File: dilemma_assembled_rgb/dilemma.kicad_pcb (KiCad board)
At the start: 4 copper layers, 130 x 91 mm, 122 parts, among them J1 USB_C_Receptacle_USB2.0, J102 Serial, J105 Conn_01x04_Female, J113 Cirque, J2 Conn_01x03_Female, J5 Conn_01x02, SW1 SW_Push, SW110 SW_SPST, SW2 SW_Push, SW3002 RotaryEncoder_Switch, U1 RP2040, U2 GD25Q80CEIGR, U3 XC6210B332MR-G, U4 USBLC6-2P6, Y1 Crystal_GND24

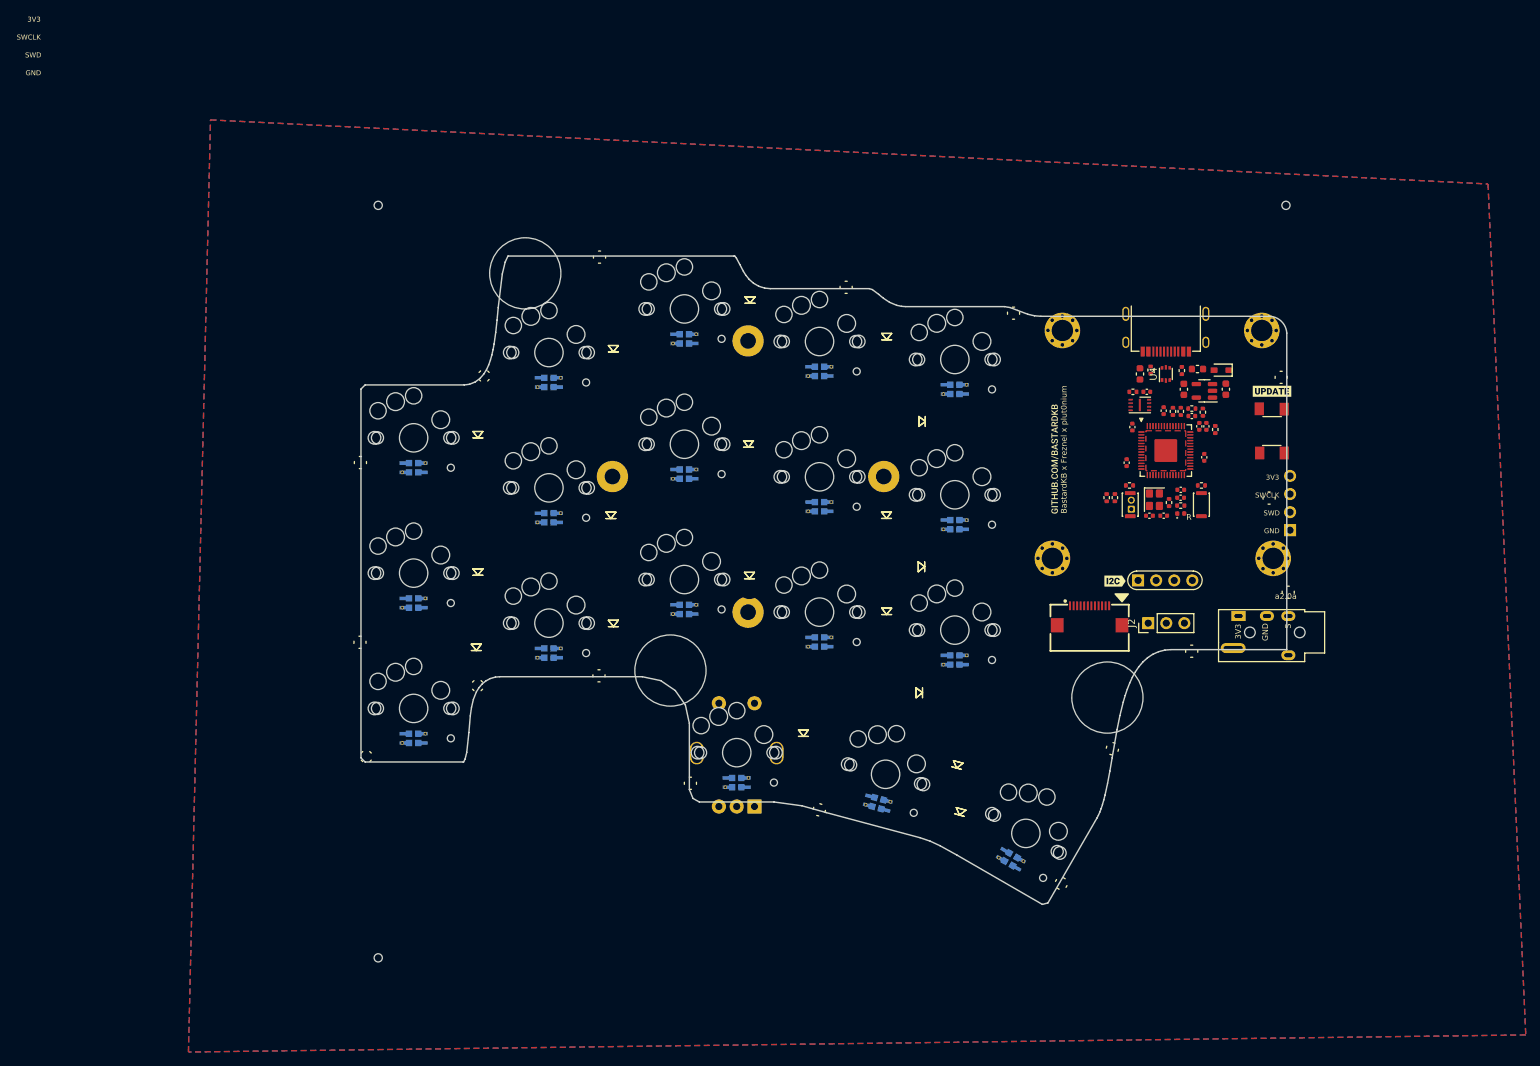
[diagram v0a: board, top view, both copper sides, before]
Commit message: move diodes
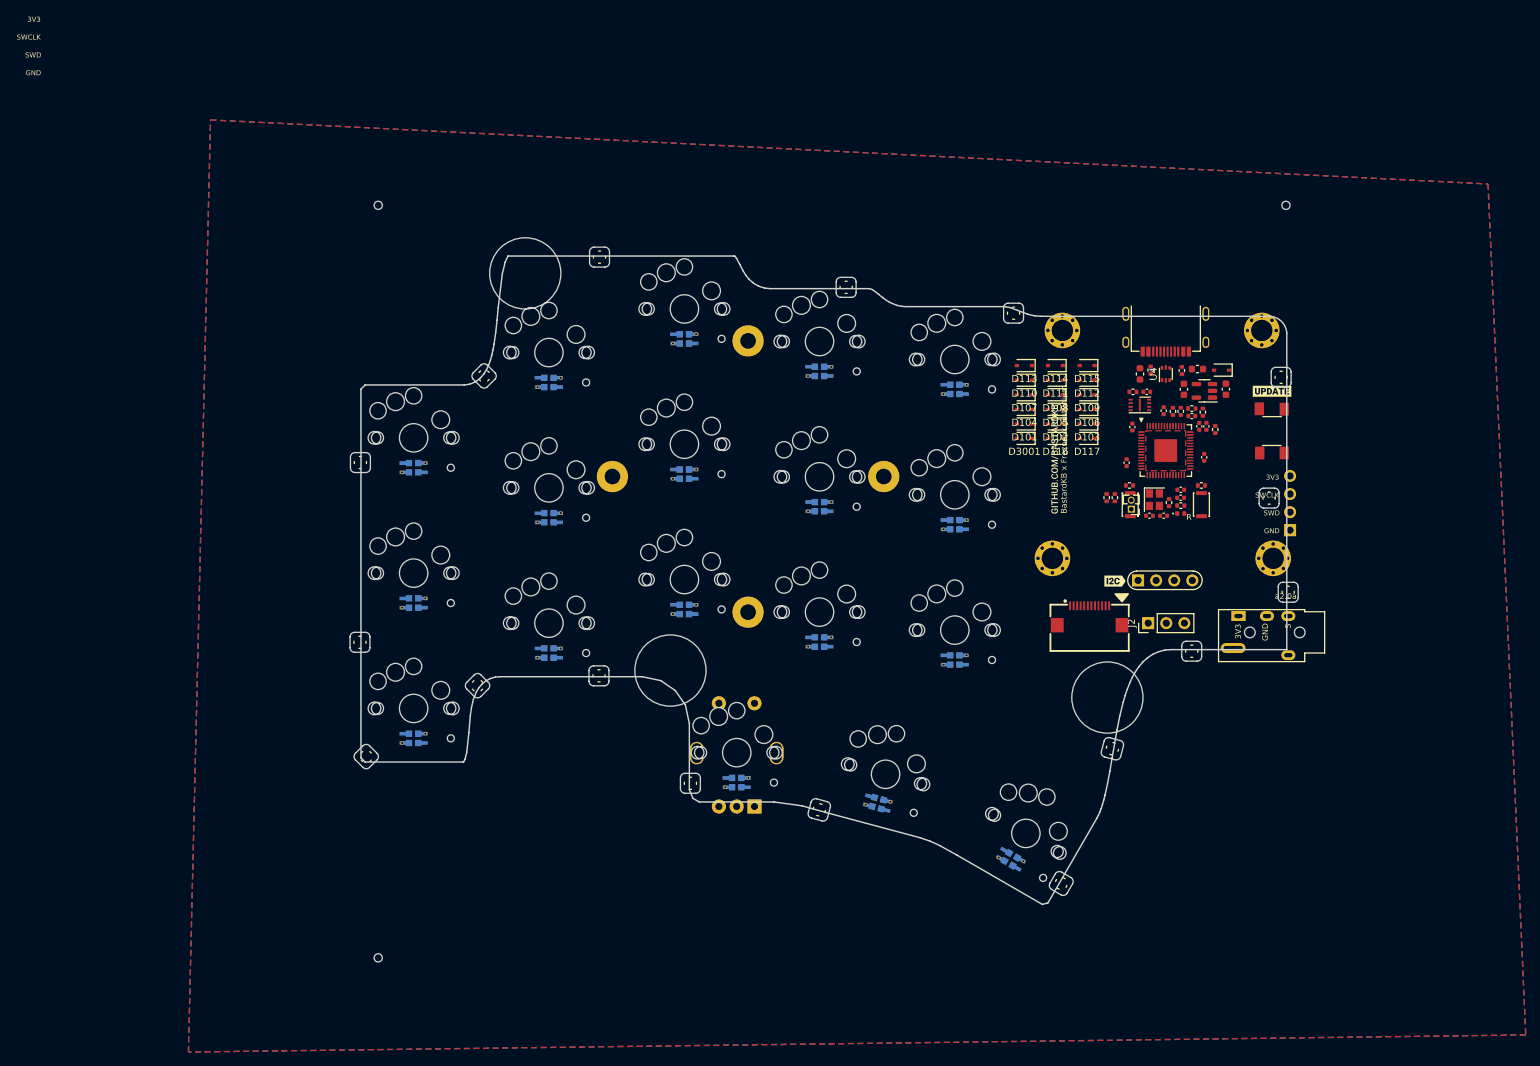
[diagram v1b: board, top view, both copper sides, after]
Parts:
- D101, D102, D103, D104, D105, D106, D107, D108, D109, D110, D111, D112, D113, D114, D115, D116, D117, D3001: footprint local-libraries:D_1206_handsolder_reversible_hole -> Diode_SMD:D_SOD-323
- G*** (x3): footprint LOGO -> local-libraries:LOGO
- moved D103 91.4 mm to (148.0, 51.8), turned to 180 degrees
- moved D102 83.8 mm to (143.6, 51.8), turned to 180 degrees
- moved D101 76.8 mm to (139.2, 51.8), turned to 180 degrees
- moved D106 73.1 mm to (148.0, 49.8), turned to 180 degrees
- moved D105 64.2 mm to (143.6, 49.8), turned to 180 degrees
- moved D104 58.4 mm to (139.2, 49.8), turned to 180 degrees
- moved D117 55.5 mm to (148.0, 53.8), turned to 180 degrees
- moved D109 53.8 mm to (148.0, 47.7), turned to 180 degrees
- moved D3001 51.8 mm to (139.2, 53.8), turned to 180 degrees
- moved D115 51.6 mm to (148.0, 43.6)
- moved D116 48.0 mm to (143.6, 53.8), turned to 180 degrees
- moved D108 43.7 mm to (143.6, 47.7), turned to 180 degrees
- moved D112 43.0 mm to (148.0, 45.6), turned to 180 degrees
- moved D107 40.8 mm to (139.2, 47.7), turned to 180 degrees
- moved D114 33.9 mm to (143.6, 43.6)
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
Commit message: add sk6805 rgb 3d model
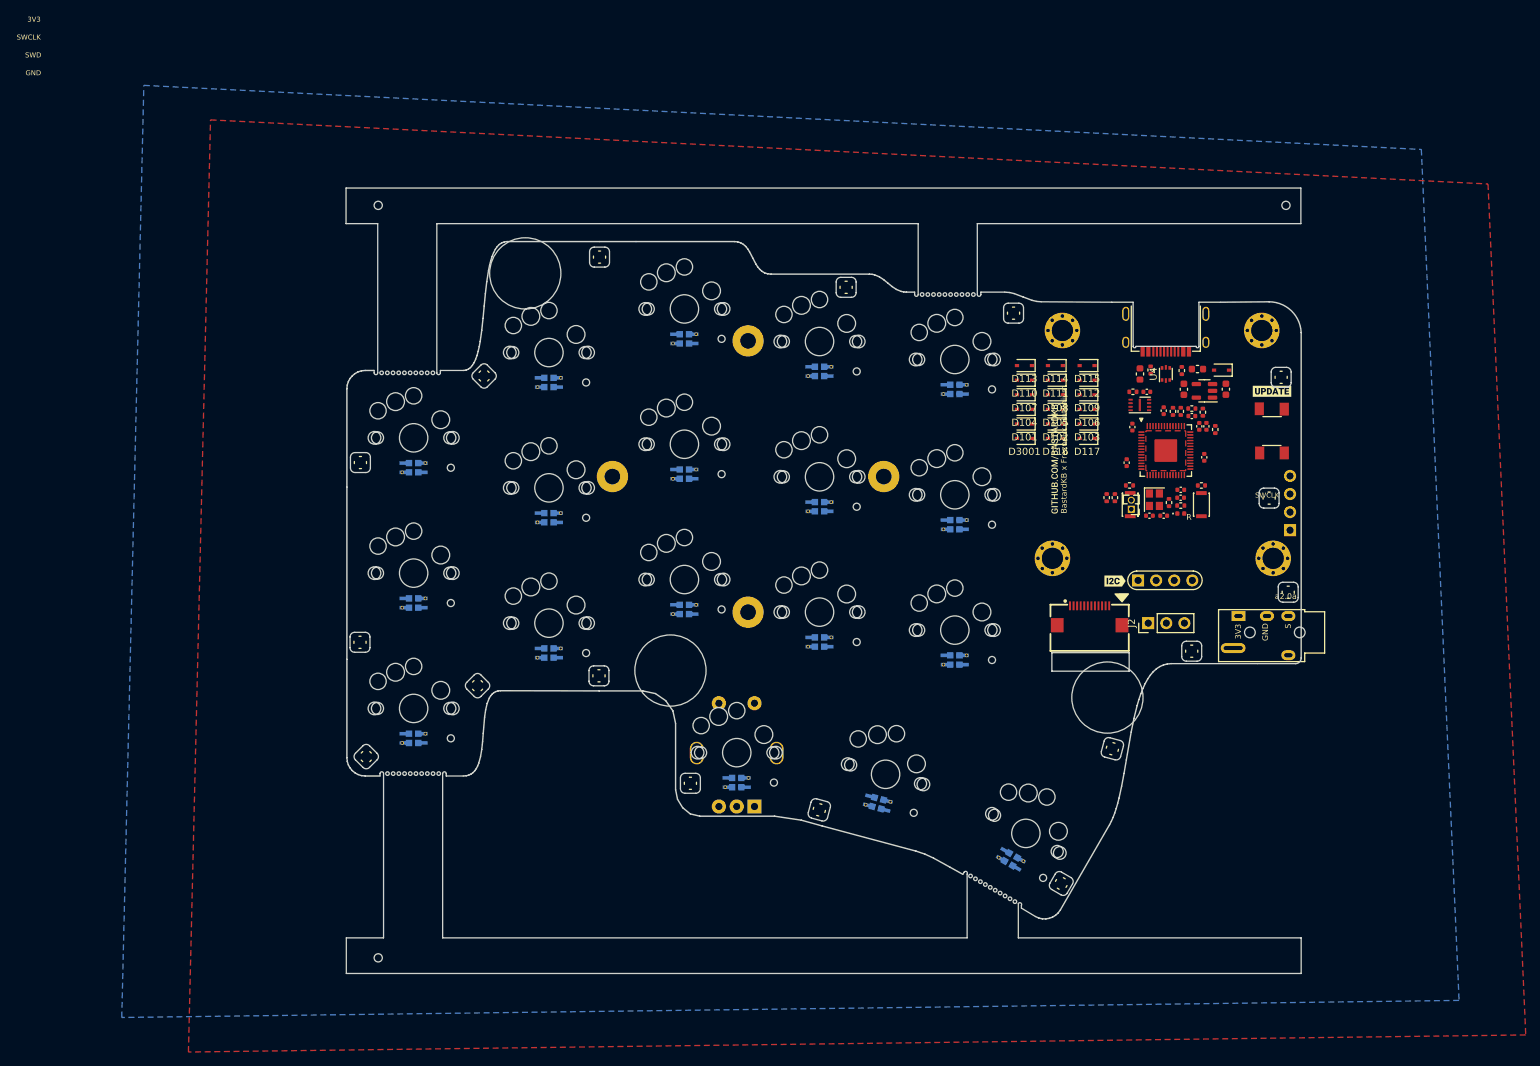
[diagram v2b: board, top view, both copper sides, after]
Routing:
- added copper zone on B.Cu, net +3V3
- removed copper zone on In1.Cu, net +3V3
- removed copper zone on B.Cu, net GND
- removed copper zone on In2.Cu, net GND
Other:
- board size 130 x 91 mm -> 134.1 x 110.3 mm
- copper layers 4 -> 2

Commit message: edge cuts
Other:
- board size 134.1 x 110.3 mm -> 134 x 95.1 mm

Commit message: edge cuts
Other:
- board size 134 x 95.1 mm -> 106.1 x 95.1 mm
